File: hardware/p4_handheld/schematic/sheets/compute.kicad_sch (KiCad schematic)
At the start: 8 parts, among them U1 ESP32-P4NRW32X, U9 QSPI-NOR-32MB, X1 40MHz-crystal

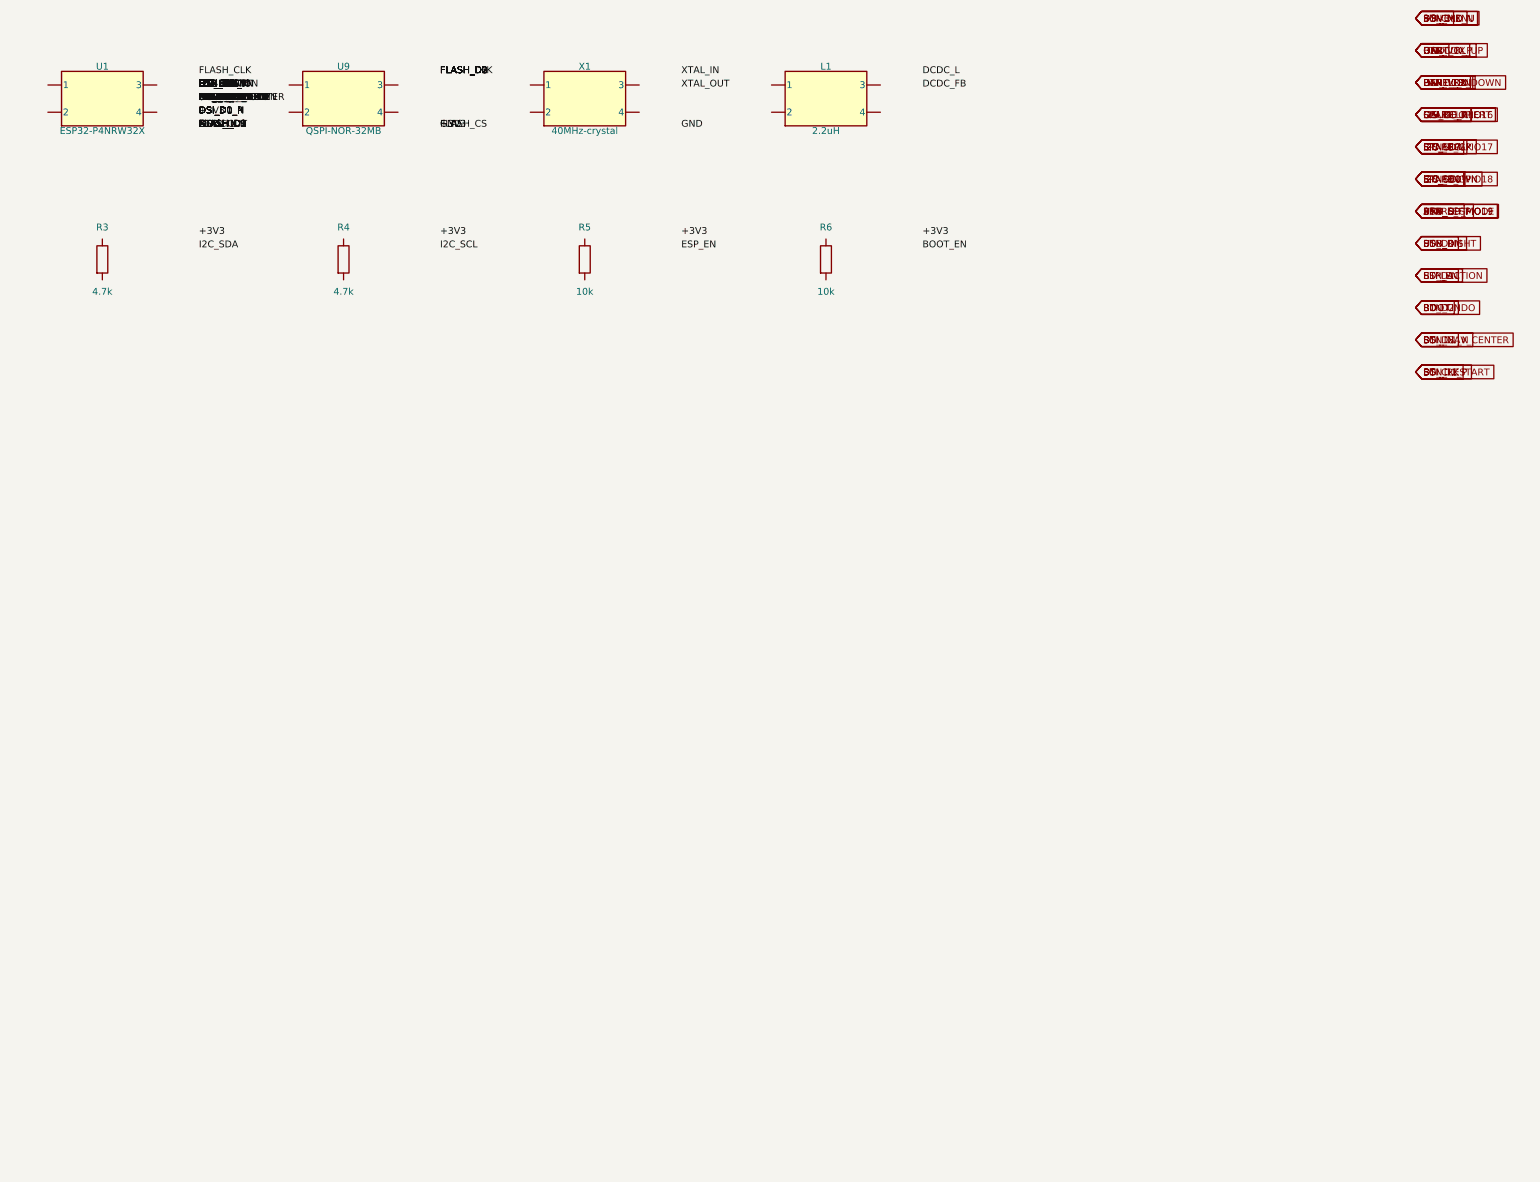
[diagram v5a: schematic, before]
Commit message: hw(p4_handheld): ERC-clean schematic engine (real pins, on-endpoint labels, project symbol lib)
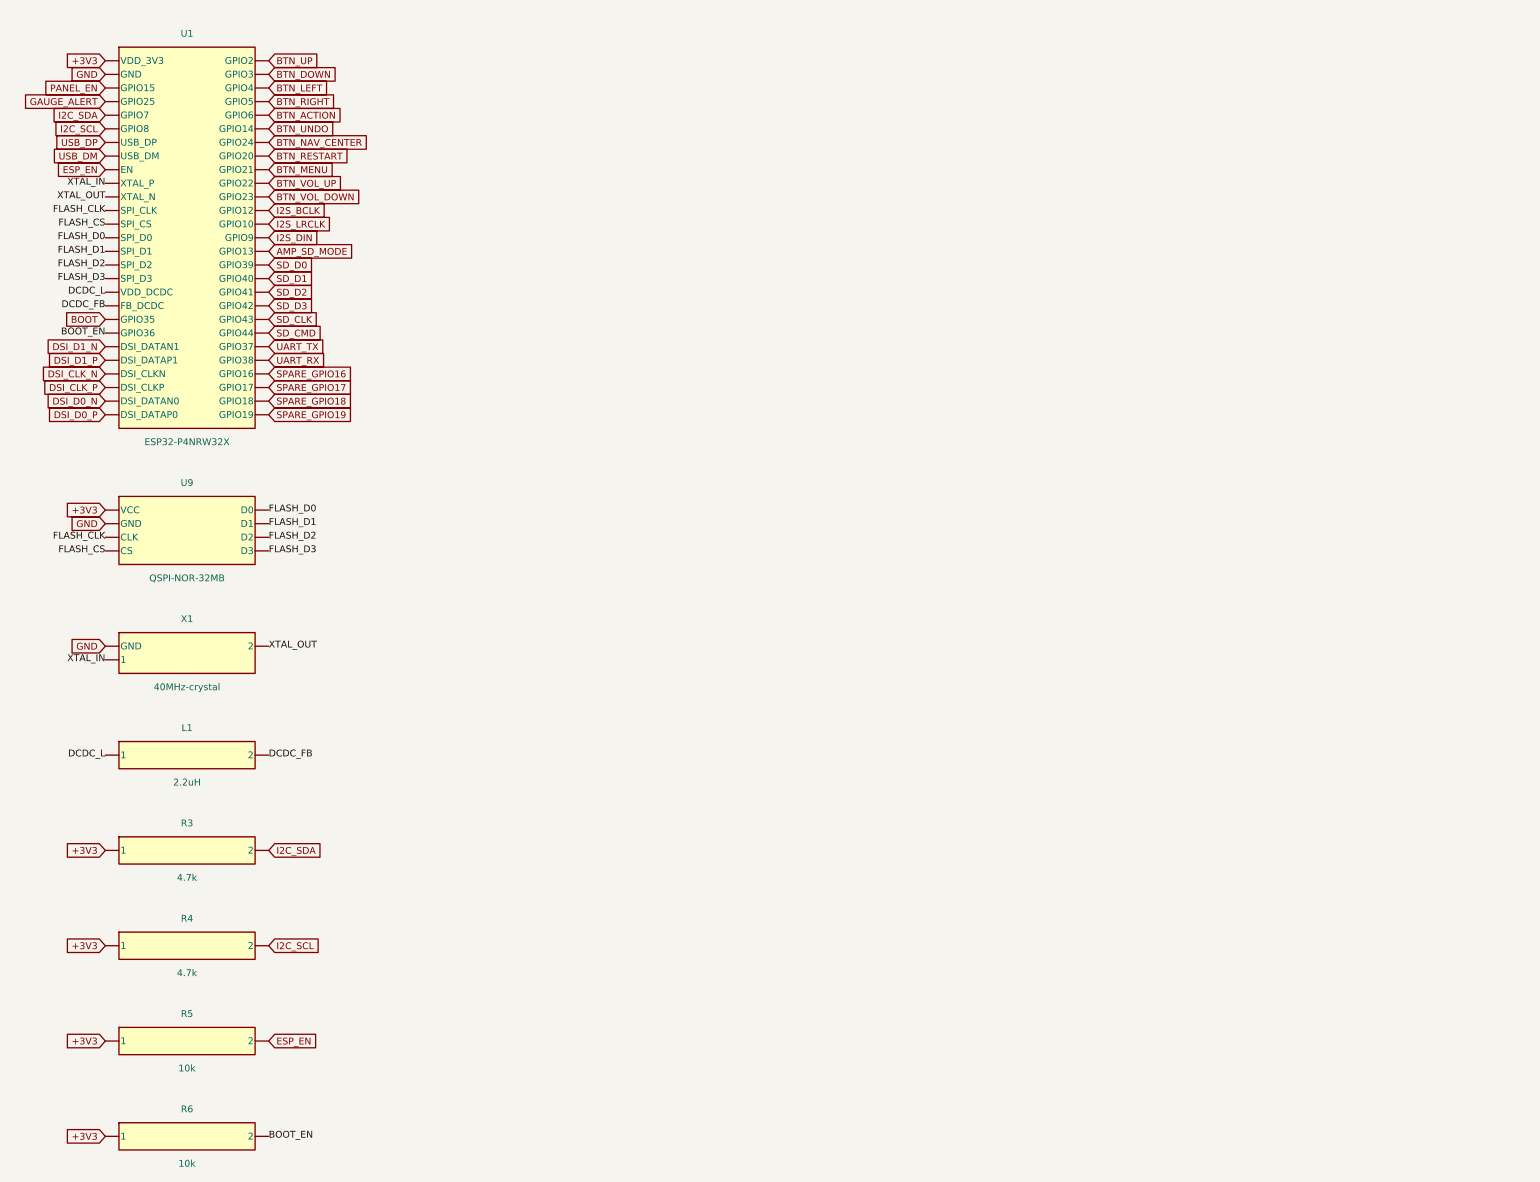
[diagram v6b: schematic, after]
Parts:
- removed L1: 2.2uH, IND-SMD_L4.0-W4.0_HPC4018BM, symbol PSP4H:Block2
- removed R3, R4: 4.7k, R0402, symbol Device:R
- removed R5, R6: 10k, R0402, symbol Device:R
- removed U1: ESP32-P4NRW32X, QFN-104_L10.0-W10.0-P0.35-TL-EP7.5, symbol PSP4H:Block2
- removed U9: QSPI-NOR-32MB, WSON-8_L8.0-W6.10-P1.27-BL-EP, symbol PSP4H:Block2
- removed X1: 40MHz-crystal, SMD3225-4P, symbol PSP4H:Block2
- added L1: 2.2uH, symbol PSP4H:SYM_L1
- added R3: 4.7k, symbol PSP4H:SYM_R3
- added R4: 4.7k, symbol PSP4H:SYM_R4
- added R5: 10k, symbol PSP4H:SYM_R5
- added R6: 10k, symbol PSP4H:SYM_R6
- added U1: ESP32-P4NRW32X, symbol PSP4H:SYM_U1
- added U9: QSPI-NOR-32MB, symbol PSP4H:SYM_U9
- added X1: 40MHz-crystal, symbol PSP4H:SYM_X1
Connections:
- net +3V3: now also R3.1, R4.1, R5.1, R6.1, U1.VDD_3V3, U9.VCC
- new net AMP_SD_MODE: U1.GPIO13
- new net BOOT: U1.GPIO35
- new net BOOT_EN: R6.2, U1.GPIO36
- new net BTN_ACTION: U1.GPIO6
- new net BTN_DOWN: U1.GPIO3
- new net BTN_LEFT: U1.GPIO4
- new net BTN_MENU: U1.GPIO21
- new net BTN_NAV_CENTER: U1.GPIO24
- new net BTN_RESTART: U1.GPIO20
- new net BTN_RIGHT: U1.GPIO5
- new net BTN_UNDO: U1.GPIO14
- new net BTN_UP: U1.GPIO2
- new net BTN_VOL_DOWN: U1.GPIO23
- new net BTN_VOL_UP: U1.GPIO22
- new net DCDC_FB: L1.2, U1.FB_DCDC
- new net DCDC_L: L1.1, U1.VDD_DCDC
- new net DSI_CLK_N: U1.DSI_CLKN
- new net DSI_CLK_P: U1.DSI_CLKP
- new net DSI_D0_N: U1.DSI_DATAN0
- new net DSI_D0_P: U1.DSI_DATAP0
- new net DSI_D1_N: U1.DSI_DATAN1
- new net DSI_D1_P: U1.DSI_DATAP1
- new net ESP_EN: R5.2, U1.EN
- new net FLASH_CLK: U1.SPI_CLK, U9.CLK
- new net FLASH_CS: U1.SPI_CS, U9.CS
- new net FLASH_D0: U1.SPI_D0, U9.D0
- new net FLASH_D1: U1.SPI_D1, U9.D1
- new net FLASH_D2: U1.SPI_D2, U9.D2
- new net FLASH_D3: U1.SPI_D3, U9.D3
- new net GAUGE_ALERT: U1.GPIO25
- new net GND: U1.GND, U9.GND, X1.GND
- new net I2C_SCL: R4.2, U1.GPIO8
- new net I2C_SDA: R3.2, U1.GPIO7
- new net I2S_BCLK: U1.GPIO12
- new net I2S_DIN: U1.GPIO9
- new net I2S_LRCLK: U1.GPIO10
- new net PANEL_EN: U1.GPIO15
- new net SD_CLK: U1.GPIO43
- new net SD_CMD: U1.GPIO44
- new net SD_D0: U1.GPIO39
- new net SD_D1: U1.GPIO40
- new net SD_D2: U1.GPIO41
- new net SD_D3: U1.GPIO42
- new net SPARE_GPIO16: U1.GPIO16
- new net SPARE_GPIO17: U1.GPIO17
- new net SPARE_GPIO18: U1.GPIO18
- new net SPARE_GPIO19: U1.GPIO19
- new net UART_RX: U1.GPIO38
- new net UART_TX: U1.GPIO37
- new net USB_DM: U1.USB_DM
- new net USB_DP: U1.USB_DP
- new net XTAL_IN: U1.XTAL_P, X1.1
- new net XTAL_OUT: U1.XTAL_N, X1.2
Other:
- title: PuzzleScript Card — compute -> PuzzleScript P4 Handheld — compute
